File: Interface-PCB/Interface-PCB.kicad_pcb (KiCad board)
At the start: 2 copper layers, 85.1 x 73.7 mm, 27 parts, among them IC1 SN74LVC245AN, IC2 TBD62783A, IC3 TBD62783A, J1 BARREL_JACK_PAD, J10 LEVEL_SENSOR, J11 LEVEL_SENSOR, J12 LEVEL_SENSOR, J13 TEMPERATURE_SENSOR, J14 TEMPERATURE_SENSOR, J2 BARREL_JACK_PAD, J3 RASPBERRYPI-40-PIN-GPIO, J4 I2C_HEADER, J5 CONN_05JST, J6 CONN_05JST, J7 LEVEL_SENSOR, J8 LEVEL_SENSOR, J9 LEVEL_SENSOR, M1 PERISTALTIC_PUMP, M2 PERISTALTIC_PUMP, M3 PERISTALTIC_PUMP, U1 TB6612FNG_BREAKOUT, U2 TB6612FNG_BREAKOUT, U3 CD74HC4067_MUX

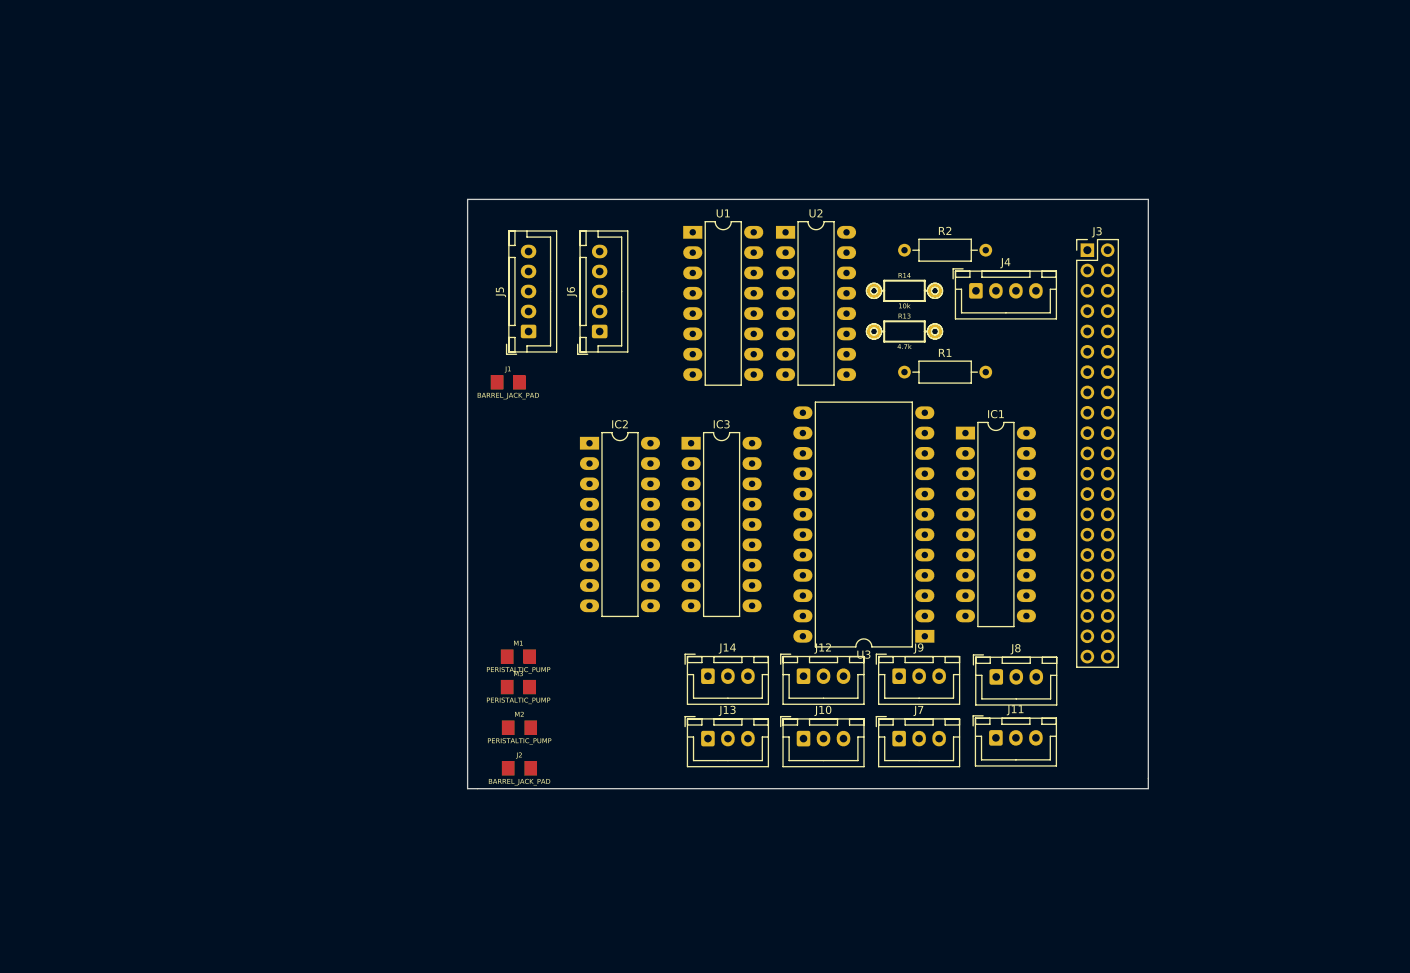
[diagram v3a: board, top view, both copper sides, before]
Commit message: Upgrade project to KiCad 6
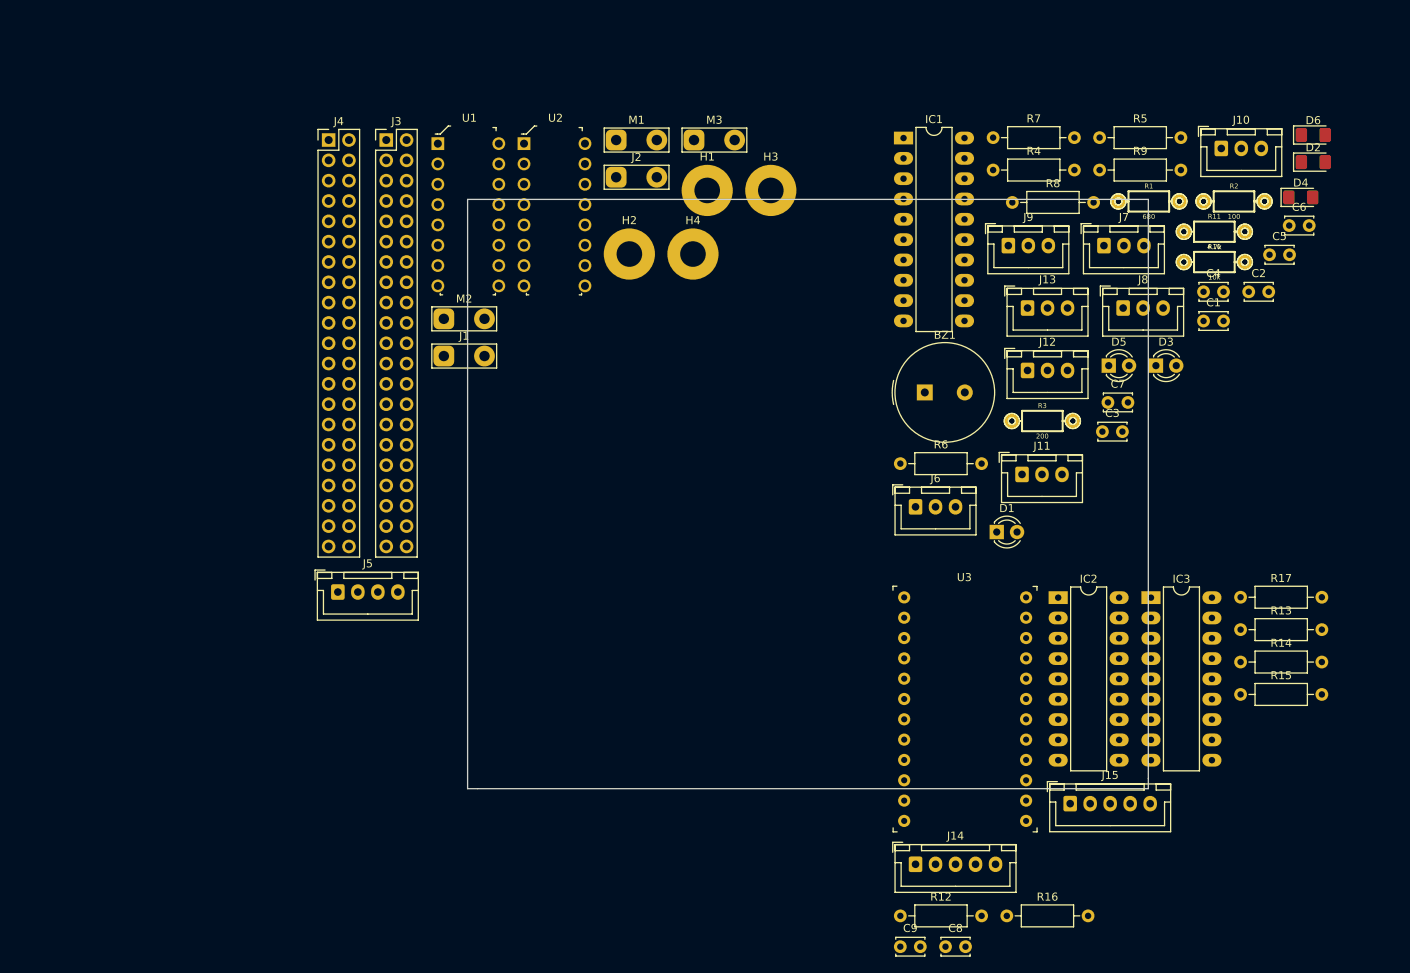
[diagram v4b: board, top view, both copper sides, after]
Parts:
- added BZ1: Buzzer, Buzzer_Beeper:Buzzer_TDK_PS1240P02BT_D12.2mm_H6.5mm, F.Cu at (177.8, 96.5)
- added C1: 10nF, Capacitor_THT:C_Disc_D3.4mm_W2.1mm_P2.50mm, F.Cu at (212.6, 87.6)
- added C2: 10nF, Capacitor_THT:C_Disc_D3.4mm_W2.1mm_P2.50mm, F.Cu at (218.3, 83.9)
- added C3: 10nF, Capacitor_THT:C_Disc_D3.4mm_W2.1mm_P2.50mm, F.Cu at (200.0, 101.4)
- added C4: 10nF, Capacitor_THT:C_Disc_D3.4mm_W2.1mm_P2.50mm, F.Cu at (212.6, 83.9)
- added C5: 10nF, Capacitor_THT:C_Disc_D3.4mm_W2.1mm_P2.50mm, F.Cu at (220.9, 79.3)
- added C6: 10nF, Capacitor_THT:C_Disc_D3.4mm_W2.1mm_P2.50mm, F.Cu at (223.4, 75.7)
- added C7: 100nF, Capacitor_THT:C_Disc_D3.4mm_W2.1mm_P2.50mm, F.Cu at (200.7, 97.8)
- added C8: 100nF, Capacitor_THT:C_Disc_D3.4mm_W2.1mm_P2.50mm, F.Cu at (180.4, 165.8)
- added C9: 100nF, Capacitor_THT:C_Disc_D3.4mm_W2.1mm_P2.50mm, F.Cu at (174.7, 165.8)
- added D1: 12V_ON, LED_THT:LED_D3.0mm, F.Cu at (186.8, 114.0)
- added D2: 12V_ON_SMD, LED_SMD:LED_1206_3216Metric_Pad1.42x1.75mm_HandSolder, F.Cu at (226.4, 67.7)
- added D3: USER_LED, LED_THT:LED_D3.0mm, F.Cu at (206.7, 93.2)
- added D4: USER_LED_SMD, LED_SMD:LED_1206_3216Metric_Pad1.42x1.75mm_HandSolder, F.Cu at (224.8, 72.1)
- added D5: 5V_ON, LED_THT:LED_D3.0mm, F.Cu at (200.8, 93.2)
- added D6: 5V_ON_SMD, LED_SMD:LED_1206_3216Metric_Pad1.42x1.75mm_HandSolder, F.Cu at (226.4, 64.3)
- added H1: MountingHole, MountingHole:MountingHole_3.2mm_M3_Pad, F.Cu at (150.6, 71.3)
- added H2: MountingHole, MountingHole:MountingHole_3.2mm_M3_Pad, F.Cu at (140.9, 79.2)
- added H3: MountingHole, MountingHole:MountingHole_3.2mm_M3_Pad, F.Cu at (158.6, 71.3)
- added H4: MountingHole, MountingHole:MountingHole_3.2mm_M3_Pad, F.Cu at (148.8, 79.2)
- added J15: CONN_05JST, Connector_JST:JST_XH_B5B-XH-A_1x05_P2.50mm_Vertical, F.Cu at (196.0, 147.9)
- added R10: 10k, Resistors:AXIAL-0.3-KIT, F.Cu at (214.0, 80.2)
- added R11: 4.7k, Resistors:AXIAL-0.3-KIT, F.Cu at (214.0, 76.4)
- added R12: 10k, Resistor_THT:R_Axial_DIN0207_L6.3mm_D2.5mm_P10.16mm_Horizontal, F.Cu at (174.7, 161.9)
- added R15: 10k, Resistor_THT:R_Axial_DIN0207_L6.3mm_D2.5mm_P10.16mm_Horizontal, F.Cu at (217.3, 134.3)
- added R16: 10k, Resistor_THT:R_Axial_DIN0207_L6.3mm_D2.5mm_P10.16mm_Horizontal, F.Cu at (188.1, 161.9)
- added R17: 10k, Resistor_THT:R_Axial_DIN0207_L6.3mm_D2.5mm_P10.16mm_Horizontal, F.Cu at (217.3, 122.1)
- added R3: 200, Resistors:AXIAL-0.3-KIT, F.Cu at (192.5, 100.1)
- added R4: 220, Resistor_THT:R_Axial_DIN0207_L6.3mm_D2.5mm_P10.16mm_Horizontal, F.Cu at (186.3, 68.7)
- added R5: 220, Resistor_THT:R_Axial_DIN0207_L6.3mm_D2.5mm_P10.16mm_Horizontal, F.Cu at (199.7, 64.7)
- added R6: 220, Resistor_THT:R_Axial_DIN0207_L6.3mm_D2.5mm_P10.16mm_Horizontal, F.Cu at (174.7, 105.4)
- added R7: 220, Resistor_THT:R_Axial_DIN0207_L6.3mm_D2.5mm_P10.16mm_Horizontal, F.Cu at (186.3, 64.7)
- added R8: 220, Resistor_THT:R_Axial_DIN0207_L6.3mm_D2.5mm_P10.16mm_Horizontal, F.Cu at (188.7, 72.8)
- added R9: 220, Resistor_THT:R_Axial_DIN0207_L6.3mm_D2.5mm_P10.16mm_Horizontal, F.Cu at (199.7, 68.7)
- J1, J2, M1, M2, M3: footprint Fuses:1206 -> TestPoint:TestPoint_2Pads_Pitch5.08mm_Drill1.3mm
- J12: value LEVEL_SENSOR -> TEMPERATURE_SENSOR
- J14: value TEMPERATURE_SENSOR -> CONN_05JST; footprint Connector_JST:JST_XH_B3B-XH-A_1x03_P2.50mm_Vertical -> Connector_JST:JST_XH_B5B-XH-A_1x05_P2.50mm_Vertical
- J3: value RASPBERRYPI-40-PIN-GPIO -> GPIO_DEBUG_HEADER
- J4: value I2C_HEADER -> RASPBERRYPI_GPIO_CONN_HEADER; footprint Connector_JST:JST_XH_B4B-XH-A_1x04_P2.50mm_Vertical -> Connector_PinHeader_2.54mm:PinHeader_2x21_P2.54mm_Vertical
- J5: value CONN_05JST -> I2C_HEADER; footprint Connector_JST:JST_XH_B5B-XH-A_1x05_P2.50mm_Vertical -> Connector_JST:JST_XH_B4B-XH-A_1x04_P2.50mm_Vertical
- J6: value CONN_05JST -> LEVEL_SENSOR; footprint Connector_JST:JST_XH_B5B-XH-A_1x05_P2.50mm_Vertical -> Connector_JST:JST_XH_B3B-XH-A_1x03_P2.50mm_Vertical
- R1: value 10k -> 680; footprint Resistor_THT:R_Axial_DIN0207_L6.3mm_D2.5mm_P10.16mm_Horizontal -> Resistors:AXIAL-0.3-KIT
- R13: value 4.7k -> 10k; footprint Resistors:AXIAL-0.3-KIT -> Resistor_THT:R_Axial_DIN0207_L6.3mm_D2.5mm_P10.16mm_Horizontal
- R14: footprint Resistors:AXIAL-0.3-KIT -> Resistor_THT:R_Axial_DIN0207_L6.3mm_D2.5mm_P10.16mm_Horizontal
- R2: value 10k -> 100; footprint Resistor_THT:R_Axial_DIN0207_L6.3mm_D2.5mm_P10.16mm_Horizontal -> Resistors:AXIAL-0.3-KIT
- U1, U2: footprint Package_DIP:DIP-16_W7.62mm_LongPads -> digikey-footprints:DIP-16_W7.62mm
- U3: footprint Package_DIP:DIP-24_W15.24mm_LongPads -> digikey-footprints:Socket_DIP-24_15.24mm_Conn
- moved J10 90.4 mm to (214.9, 66.0)
- moved J3 88.7 mm to (110.5, 65.0)
- moved J4 83.1 mm to (103.3, 65.0)
- moved J2 74.9 mm to (139.2, 69.6)
- moved M3 71.8 mm to (149.0, 65.0)
- moved J13 67.0 mm to (190.6, 86.0)
- moved J7 66.7 mm to (200.2, 78.2)
- moved M1 65.7 mm to (139.2, 65.0)
- moved R14 62.6 mm to (217.3, 130.2)
- moved IC2 61.7 mm to (194.5, 122.2)
- moved IC3 60.6 mm to (206.1, 122.2)
- moved R13 56.2 mm to (217.3, 126.2)
- moved J9 55.5 mm to (188.2, 78.2)
- moved M2 52.0 mm to (117.7, 87.3)
- moved J8 48.8 mm to (202.6, 86.0)
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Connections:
- IC1 pad 10: 3.3V -> GND
- IC1 pad 11: Net-(IC1-Pad11) -> unconnected-(IC1-Pad11)
- IC1 pad 12: Net-(IC1-Pad12) -> unconnected-(IC1-Pad12)
- IC1 pad 19: 3.3V -> GND
- IC1 pad 8: 3.3V -> GND
- IC1 pad 9: 3.3V -> GND
- IC2 pad 10: 3.3V -> GND
- IC2 pad 11: Net-(IC2-Pad11) -> unconnected-(IC2-Pad11)
- IC2 pad 12: Net-(IC2-Pad12) -> unconnected-(IC2-Pad12)
- IC2 pad 13: Net-(IC2-Pad13) -> unconnected-(IC2-Pad13)
- IC2 pad 6: 3.3V -> GND
- IC2 pad 7: 3.3V -> GND
- IC2 pad 8: 3.3V -> GND
- IC3 pad 10: 3.3V -> GND
- IC3 pad 11: Net-(IC3-Pad11) -> unconnected-(IC3-Pad11)
- IC3 pad 12: Net-(IC3-Pad12) -> unconnected-(IC3-Pad12)
- IC3 pad 13: Net-(IC3-Pad13) -> unconnected-(IC3-Pad13)
- IC3 pad 6: 3.3V -> GND
- IC3 pad 7: 3.3V -> GND
- IC3 pad 8: 3.3V -> GND
- J1 pad 2: 3.3V -> GND
- J10 pad 2: LEVEL_PH_UP -> LEVEL_PH_DOWN
- J10 pad 3: 3.3V -> GND
- J11 pad 2: LEVEL_PH_DOWN -> LEVEL_TRAY_TOP
- J11 pad 3: 3.3V -> GND
- J12 pad 1: +5V -> +3V3
- J12 pad 2: LEVEL_TRAY_TOP -> AIR_TEMP_DATA
- J12 pad 3: 3.3V -> GND
- J13 pad 2: AIR_TEMP_DATA -> WATER_TEMP_DATA
- J13 pad 3: 3.3V -> GND
- J14 pad 1: +3V3 -> Net-(IC2-Pad18)
- J14 pad 2: WATER_TEMP_DATA -> Net-(IC2-Pad17)
- J14 pad 3: 3.3V -> Net-(IC2-Pad16)
- J2 pad 2: 3.3V -> GND
- J3 pad 10: /Remote Transistor SubSystem/SEL_0 -> MUX_SEL0
- J3 pad 14: Net-(J3-Pad14) -> GND
- J3 pad 16: /Remote Transistor SubSystem/SEL_1 -> MUX_SEL1
- J3 pad 17: Net-(J3-Pad17) -> +3V3
- J3 pad 18: /Remote Transistor SubSystem/SEL_2 -> MUX_SEL2
- J3 pad 20: Net-(J3-Pad20) -> GND
- J3 pad 22: /Remote Transistor SubSystem/SEL_3 -> MUX_SEL3
- J3 pad 25: Net-(J3-Pad25) -> GND
- J3 pad 30: Net-(J3-Pad30) -> GND
- J3 pad 34: Net-(J3-Pad34) -> GND
- J3 pad 39: 3.3V -> GND
- J3 pad 4: Net-(J3-Pad4) -> +5V
- J3 pad 6: Net-(J3-Pad6) -> GND
- J3 pad 8: /Remote Transistor SubSystem/EN -> MUX_EN
- J3 pad 9: Net-(J3-Pad9) -> GND
- J4 pad 2: I2C_SDA -> +5V
- J4 pad 3: I2C_SCL -> I2C_SDA
- J4 pad 4: (no net) -> +5V
- J5 pad 1: Net-(IC2-Pad14) -> +3V3
- J5 pad 2: Net-(IC2-Pad15) -> I2C_SDA
- J5 pad 3: Net-(IC2-Pad16) -> I2C_SCL
- J5 pad 4: Net-(IC2-Pad17) -> GND
- J6 pad 1: Net-(IC3-Pad14) -> +5V
- J6 pad 2: Net-(IC3-Pad15) -> LEVEL_WATER
- J6 pad 3: Net-(IC3-Pad16) -> GND
- J7 pad 2: LEVEL_WATER -> LEVEL_EC
- J7 pad 3: 3.3V -> GND
- J8 pad 2: LEVEL_EC -> LEVEL_TRAY_BOTTOM
- J8 pad 3: 3.3V -> GND
- J9 pad 2: LEVEL_TRAY_BOTTOM -> LEVEL_PH_UP
- J9 pad 3: 3.3V -> GND
- U1 pad 16: 3.3V -> GND
- U1 pad 3: Net-(U1-Pad3) -> GND
- U1 pad 7: (no net) -> Net-(M2-Pad6)
- U1 pad 8: Net-(U1-Pad8) -> GND
- U2 pad 13: 3.3V -> GND
- U2 pad 14: 3.3V -> GND
- U2 pad 16: 3.3V -> GND
- U2 pad 3: Net-(U2-Pad3) -> GND
- U2 pad 6: Net-(U2-Pad6) -> unconnected-(U2-Pad6)
- U2 pad 7: (no net) -> unconnected-(U2-Pad7)
- U2 pad 8: Net-(U2-Pad8) -> GND
- U3 pad 1: Net-(R2-PadP$2) -> Net-(R12-PadP$1)
- U3 pad 10: OUTLET_5_ON -> OUTLET_1_OFF
- U3 pad 11: OUTLET_1_OFF -> OUTLET_5_ON
- U3 pad 12: OUTLET_2_OFF -> OUTLET_4_ON
- U3 pad 13: OUTLET_3_OFF -> OUTLET_3_ON
- U3 pad 14: OUTLET_4_OFF -> OUTLET_2_ON
- U3 pad 15: OUTLET_5_OFF -> OUTLET_1_ON
- U3 pad 17: 3.3V -> GND
- U3 pad 19: /Remote Transistor SubSystem/EN -> MUX_EN
- U3 pad 2: Net-(R2-PadP$2) -> Net-(R13-PadP$1)
- U3 pad 20: /Remote Transistor SubSystem/SEL_0 -> MUX_SEL0
- U3 pad 21: /Remote Transistor SubSystem/SEL_1 -> MUX_SEL1
- U3 pad 22: /Remote Transistor SubSystem/SEL_2 -> MUX_SEL2
- U3 pad 23: /Remote Transistor SubSystem/SEL_3 -> MUX_SEL3
- U3 pad 3: Net-(R2-PadP$2) -> Net-(R14-PadP$1)
- U3 pad 4: Net-(R2-PadP$2) -> Net-(R15-PadP$1)
- U3 pad 5: Net-(R2-PadP$2) -> Net-(R16-PadP$1)
- U3 pad 6: OUTLET_1_ON -> OUTLET_5_OFF
- U3 pad 7: OUTLET_2_ON -> OUTLET_4_OFF
- U3 pad 8: OUTLET_3_ON -> OUTLET_3_OFF
- U3 pad 9: OUTLET_4_ON -> OUTLET_2_OFF
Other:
- net class Default removed

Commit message: Update schematic based on breadboard tests
- Add current limiting resistors to Level Shifter output
- Add pull down resistors on all Mux outputs
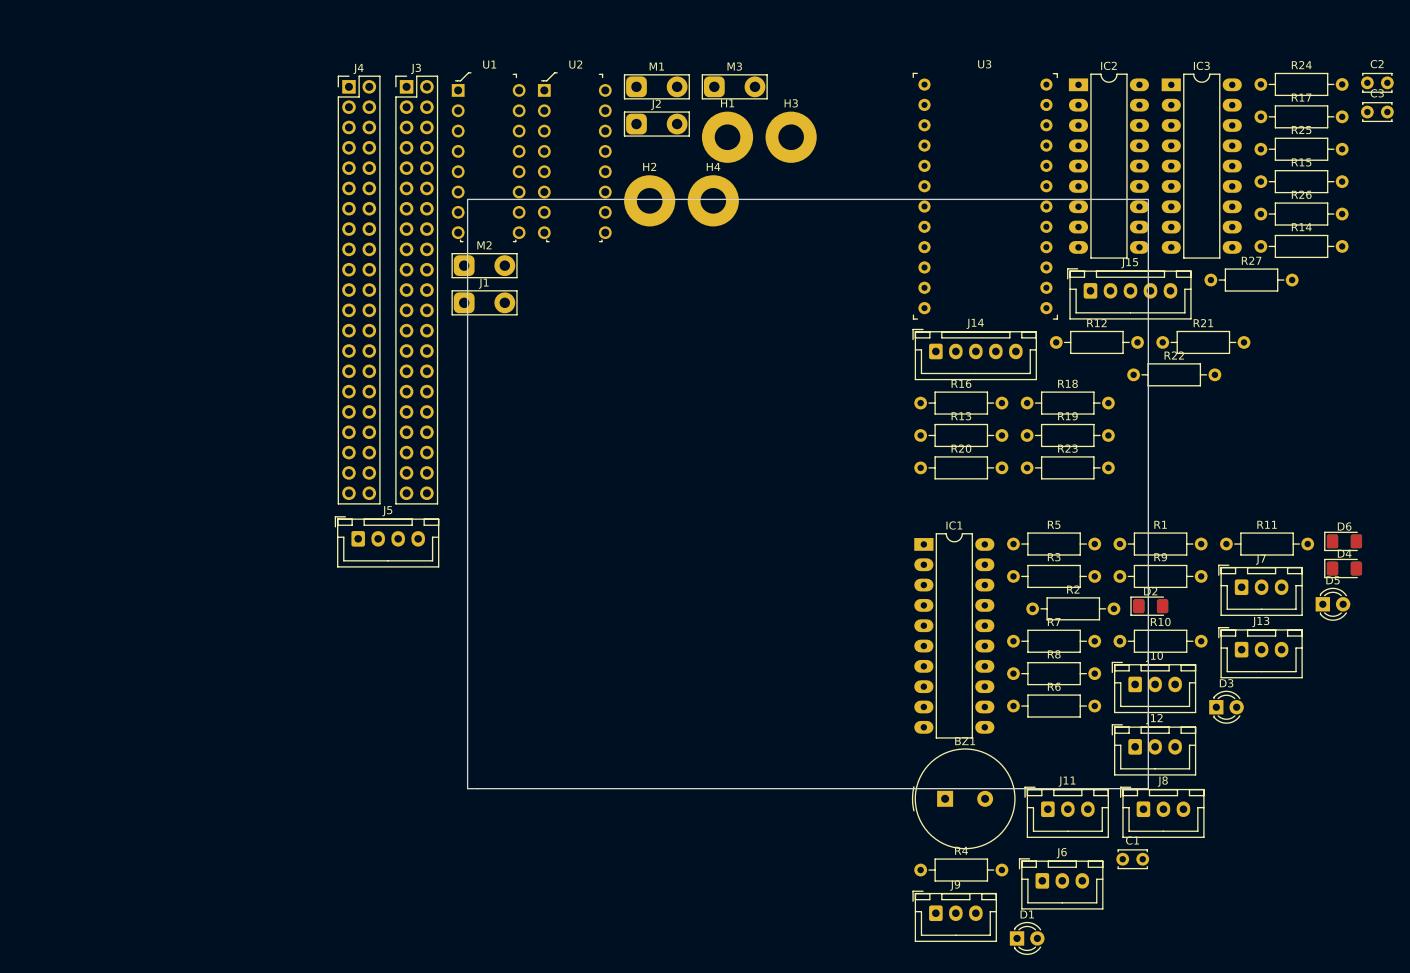
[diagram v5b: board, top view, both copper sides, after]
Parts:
- removed C4, C5, C6: 10nF, Capacitor_THT:C_Disc_D3.4mm_W2.1mm_P2.50mm
- removed C7, C8, C9: 100nF, Capacitor_THT:C_Disc_D3.4mm_W2.1mm_P2.50mm
- added R18: 10k, Resistor_THT:R_Axial_DIN0207_L6.3mm_D2.5mm_P10.16mm_Horizontal, F.Cu at (190.6, 97.8)
- added R19: 10k, Resistor_THT:R_Axial_DIN0207_L6.3mm_D2.5mm_P10.16mm_Horizontal, F.Cu at (190.6, 101.9)
- added R20: 10k, Resistor_THT:R_Axial_DIN0207_L6.3mm_D2.5mm_P10.16mm_Horizontal, F.Cu at (177.3, 106.0)
- added R21: 10k, Resistor_THT:R_Axial_DIN0207_L6.3mm_D2.5mm_P10.16mm_Horizontal, F.Cu at (207.5, 90.3)
- added R22: 10k, Resistor_THT:R_Axial_DIN0207_L6.3mm_D2.5mm_P10.16mm_Horizontal, F.Cu at (203.9, 94.3)
- added R23: 10k, Resistor_THT:R_Axial_DIN0207_L6.3mm_D2.5mm_P10.16mm_Horizontal, F.Cu at (190.6, 106.0)
- added R24: 10k, Resistor_THT:R_Axial_DIN0207_L6.3mm_D2.5mm_P10.16mm_Horizontal, F.Cu at (219.8, 58.0)
- added R25: 10k, Resistor_THT:R_Axial_DIN0207_L6.3mm_D2.5mm_P10.16mm_Horizontal, F.Cu at (219.8, 66.1)
- added R26: 10k, Resistor_THT:R_Axial_DIN0207_L6.3mm_D2.5mm_P10.16mm_Horizontal, F.Cu at (219.8, 74.2)
- added R27: 10k, Resistor_THT:R_Axial_DIN0207_L6.3mm_D2.5mm_P10.16mm_Horizontal, F.Cu at (213.6, 82.5)
- C1, C2, C3: value 10nF -> 100nF
- R1, R2, R3: footprint Resistors:AXIAL-0.3-KIT -> Resistor_THT:R_Axial_DIN0207_L6.3mm_D2.5mm_P10.16mm_Horizontal
- R10: value 10k -> 220; footprint Resistors:AXIAL-0.3-KIT -> Resistor_THT:R_Axial_DIN0207_L6.3mm_D2.5mm_P10.16mm_Horizontal
- R11: value 4.7k -> 220; footprint Resistors:AXIAL-0.3-KIT -> Resistor_THT:R_Axial_DIN0207_L6.3mm_D2.5mm_P10.16mm_Horizontal
- R4, R5: value 220 -> 10k
- moved R4 88.0 mm to (177.3, 156.2)
- moved J9 83.9 mm to (179.2, 161.6)
- moved R12 74.3 mm to (194.2, 90.3)
- moved C1 68.0 mm to (202.5, 154.9)
- moved J10 67.9 mm to (204.1, 133.0)
- moved R16 65.0 mm to (177.3, 97.8)
- moved R15 64.2 mm to (219.8, 70.2)
- moved IC2 64.2 mm to (197.0, 58.1)
- moved IC3 64.2 mm to (208.6, 58.1)
- moved J14 64.2 mm to (179.2, 91.4)
- moved J15 64.2 mm to (198.5, 83.8)
- moved U3 64.2 mm to (177.8, 58.0)
- moved R7 63.0 mm to (188.9, 127.6)
- moved J8 62.7 mm to (205.1, 148.6)
- moved R17 60.1 mm to (219.8, 62.1)
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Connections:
- C1 pad 1: unconnected-(C1-Pad1) -> +3V3
- C1 pad 2: unconnected-(C1-Pad2) -> GND
- C2 pad 1: unconnected-(C2-Pad1) -> +12V
- C2 pad 2: unconnected-(C2-Pad2) -> GND
- C3 pad 1: unconnected-(C3-Pad1) -> +12V
- C3 pad 2: unconnected-(C3-Pad2) -> GND
- IC1 pad 13: LEVEL_TRAY_BOTTOM_3V3 -> Net-(IC1-Pad13)
- IC1 pad 14: LEVEL_TRAY_TOP_3V3 -> Net-(IC1-Pad14)
- IC1 pad 15: LEVEL_EC_3V3 -> Net-(IC1-Pad15)
- IC1 pad 16: LEVEL_PH_DOWN_3V3 -> Net-(IC1-Pad16)
- IC1 pad 17: LEVEL_PH_UP_3V3 -> Net-(IC1-Pad17)
- IC1 pad 18: LEVEL_WATER_3V3 -> Net-(IC1-Pad18)
- R12 pad 1: (no net) -> Net-(R12-Pad1)
- R12 pad 2: (no net) -> GND
- R13 pad 1: (no net) -> Net-(R13-Pad1)
- R13 pad 2: (no net) -> GND
- R14 pad 1: (no net) -> Net-(R14-Pad1)
- R14 pad 2: (no net) -> GND
- R15 pad 1: (no net) -> Net-(R15-Pad1)
- R15 pad 2: (no net) -> GND
- R16 pad 1: (no net) -> Net-(R16-Pad1)
- R16 pad 2: (no net) -> GND
- R17 pad 1: (no net) -> OUTLET_5_OFF
- R17 pad 2: (no net) -> GND
- R4 pad 1: (no net) -> AIR_TEMP_DATA
- R4 pad 2: (no net) -> +3V3
- R5 pad 1: (no net) -> WATER_TEMP_DATA
- R5 pad 2: (no net) -> +3V3
- R6 pad 1: (no net) -> LEVEL_WATER_3V3
- R6 pad 2: (no net) -> Net-(IC1-Pad18)
- R7 pad 1: (no net) -> LEVEL_PH_UP_3V3
- R7 pad 2: (no net) -> Net-(IC1-Pad17)
- R8 pad 1: (no net) -> LEVEL_PH_DOWN_3V3
- R8 pad 2: (no net) -> Net-(IC1-Pad16)
- R9 pad 1: (no net) -> LEVEL_EC_3V3
- R9 pad 2: (no net) -> Net-(IC1-Pad15)
- U3 pad 1: Net-(R12-PadP$1) -> Net-(R12-Pad1)
- U3 pad 2: Net-(R13-PadP$1) -> Net-(R13-Pad1)
- U3 pad 3: Net-(R14-PadP$1) -> Net-(R14-Pad1)
- U3 pad 4: Net-(R15-PadP$1) -> Net-(R15-Pad1)
- U3 pad 5: Net-(R16-PadP$1) -> Net-(R16-Pad1)
